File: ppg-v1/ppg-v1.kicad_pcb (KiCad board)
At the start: 2 copper layers, 31 x 36.6 mm, 56 parts, among them J1 USB_microB_2040002-1, J2 Conn_01x04_Male, SW1 SW_Push, SW2 SW_Push, SW3 PCM12, U1 STM32F411CEUx, U2 MCP73831T-2ACI/OT, U3 Opamp_Dual_Generic, U4 Opamp_Dual_Generic, U5 TPS2113APW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

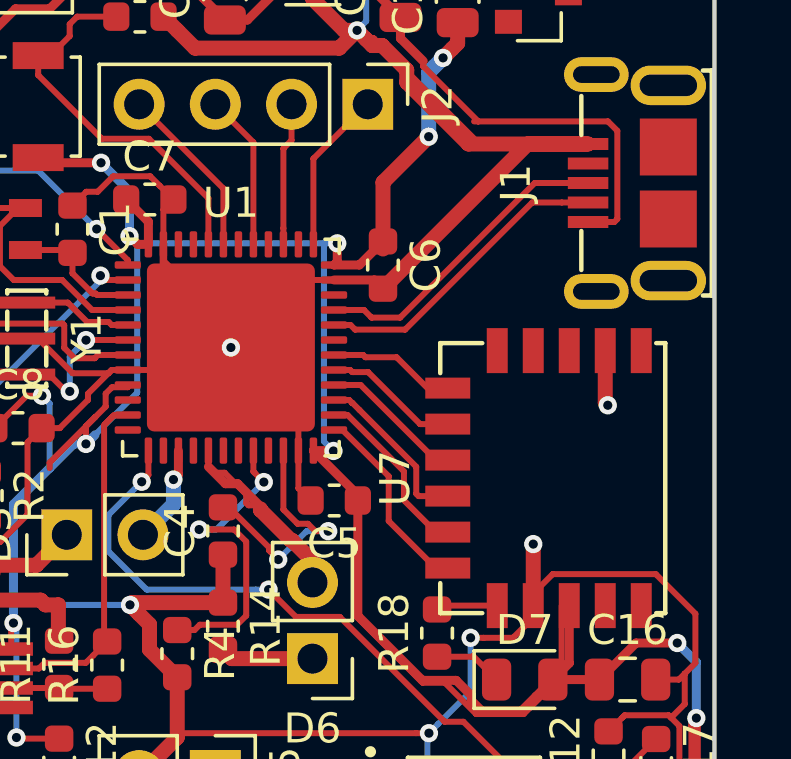
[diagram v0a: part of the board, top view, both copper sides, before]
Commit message: Connect hardware serial pins on stm32 to Bluetooth module
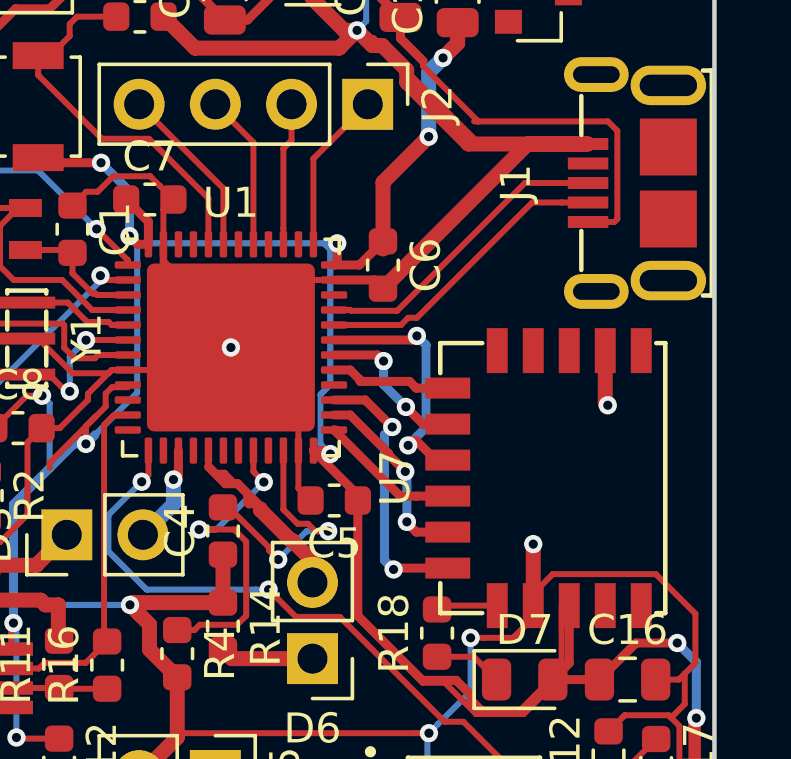
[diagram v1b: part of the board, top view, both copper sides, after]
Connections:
- U1 pad 25: /CTS -> /RTS
- U1 pad 27: /RTS -> /CTS
- U1 pad 28: /TX -> Net-(U1-Pad28)
- U1 pad 29: /RX -> /RX_IND
- U1 pad 30: /RX_IND -> /RX
- U1 pad 31: Net-(U1-Pad31) -> /TX
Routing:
- net /TX: track 4.83 -> 8.49 mm, vias 0 -> 2
- net /CTS: track 6.57 -> 9.12 mm, vias 0 -> 2
- net /RTS: track 5.65 -> 4.77 mm
- net /RST_N: track 5.97 -> 6.80 mm, vias 0 -> 2
- net /RX: track 4.54 -> 5.20 mm, vias 0 -> 2
